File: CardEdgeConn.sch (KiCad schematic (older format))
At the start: 5 parts, among them J5 5-5530843-4, J6 Conn_01x03, J7 302-S101

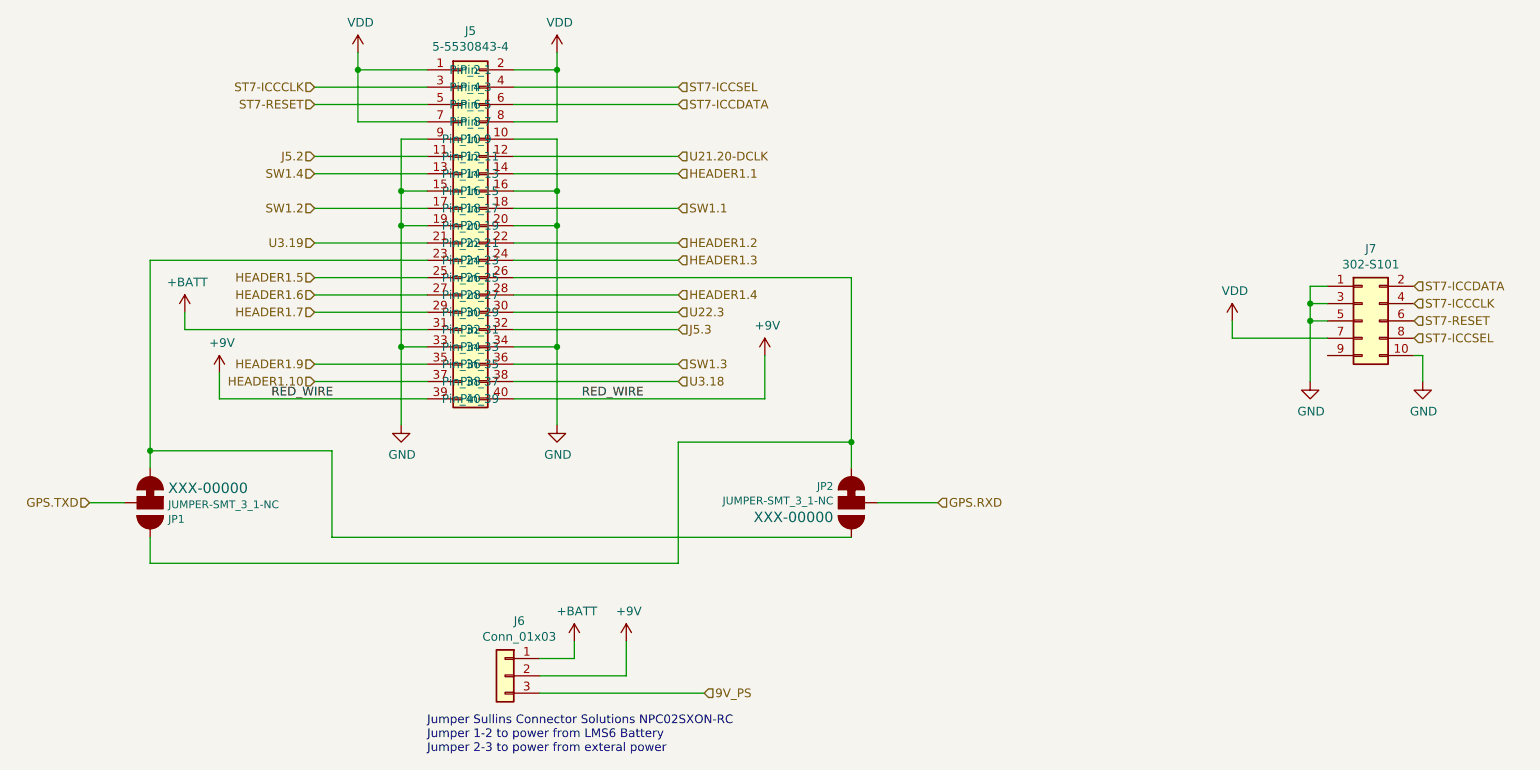
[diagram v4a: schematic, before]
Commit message: eFuse added
Added eFuse, LEDs, and addtional power configuration options.
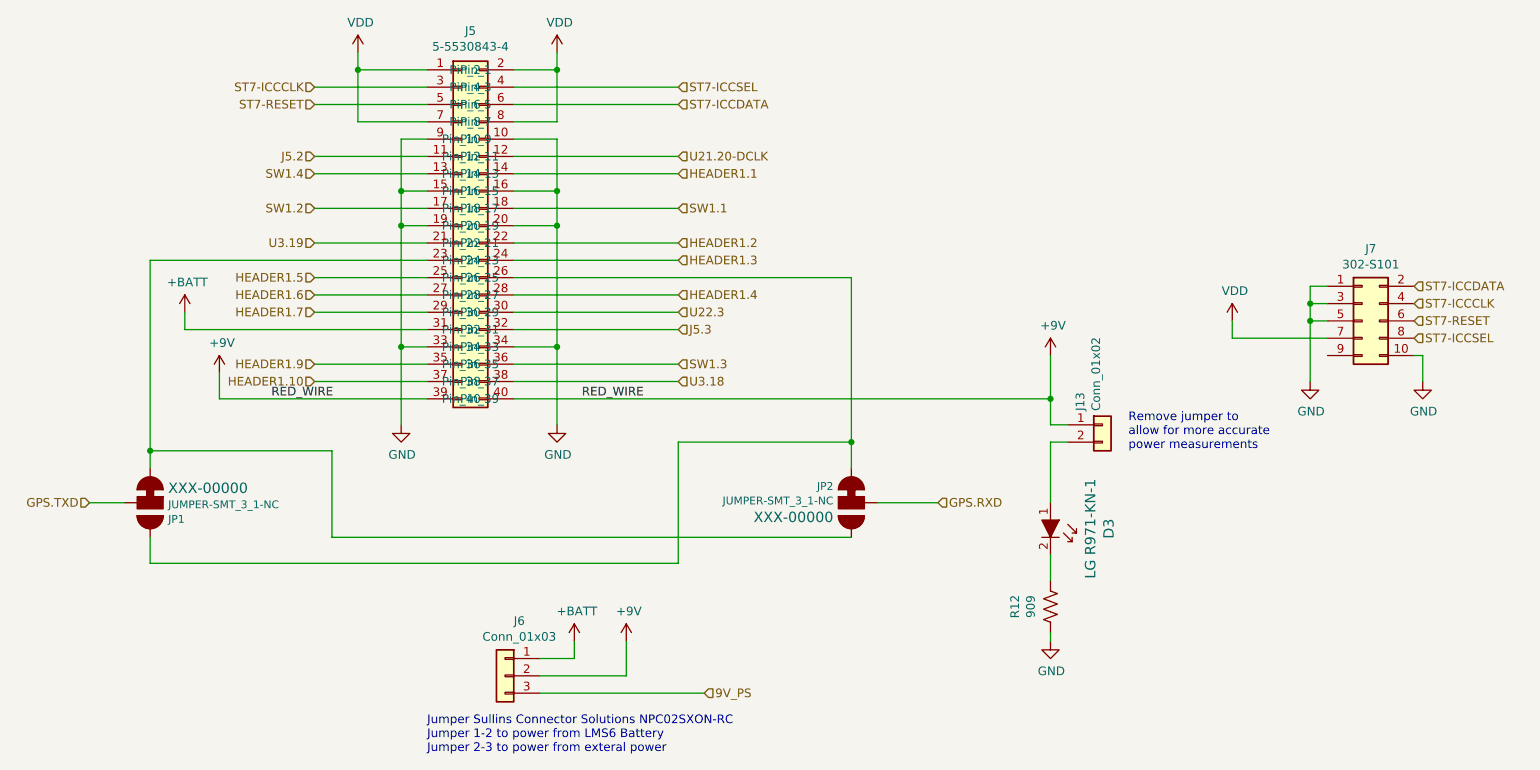
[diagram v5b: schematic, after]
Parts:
- added D3: LG R971-KN-1, digikey-footprints:0805, symbol dk_LED-Indication-Discrete:LH_R974-LP-1
- added J13: Conn_01x02, Connector_PinHeader_2.54mm:PinHeader_1x02_P2.54mm_Vertical, symbol Connector_Generic:Conn_01x02
- added R12: 909, Resistor_SMD:R_0805_2012Metric_Pad1.20x1.40mm_HandSolder, symbol Device:R_US
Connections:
- net +9V: now also J13.1 (Pin_1)
- net GND: now also R12.2
- new net: D3.1, J13.2 (Pin_2)
- new net: D3.2, R12.1
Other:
- note added: "Remove jumper to \nallow for more accurate\npower measurements"
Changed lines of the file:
@@
 $Descr A4 11693 8268
 encoding utf-8
-Sheet 4 4
-Title ""
-Date ""
-Rev ""
+Sheet 4 5
+Title "Card Connector"
+Date "2020-10-17"
+Rev "2"
 Comp ""
 Comment1 ""
@@
 L power:+9V #PWR?
 U 1 1 5F7D0952
-P 4850 2850
+P 6500 2850
 AR Path="/5F7D0952" Ref="#PWR?"  Part="1"
 AR Path="/5F7BE189/5F7D0952" Ref="#PWR?"  Part="1"
 AR Path="/5F7C6408/5F7D0952" Ref="#PWR0101"  Part="1"
-F 0 "#PWR0101" H 4850 2700 50  0001 C CNN
-F 1 "+9V" H 4865 3023 50  0000 C CNN
-F 2 "" H 4850 2850 50  0001 C CNN
-F 3 "" H 4850 2850 50  0001 C CNN
-	1    4850 2850
-	1    0    0    -1
-$EndComp
-Wire Wire Line
-	4850 3100 4850 2850
+F 0 "#PWR0101" H 6500 2700 50  0001 C CNN
+F 1 "+9V" H 6515 3023 50  0000 C CNN
+F 2 "" H 6500 2850 50  0001 C CNN
+F 3 "" H 6500 2850 50  0001 C CNN
+	1    6500 2850
+	1    0    0    -1
+$EndComp
+Wire Wire Line
+	6500 3100 6500 2850
 Wire Wire Line
 	4350 2600 3400 2600
@@
 Text Label 4150 3100 2    50   ~ 0
 RED_WIRE
-Wire Wire Line
-	3400 3100 4850 3100
 Wire Wire Line
 	4350 1300 3400 1300
@@
 Wire Wire Line
 	5350 3350 5350 2400
+Wire Wire Line
+	3400 3100 6500 3100
+$Comp
+L dk_LED-Indication-Discrete:LH_R974-LP-1 D?
+U 1 1 5F959F13
+P 6500 3900
+AR Path="/5F917C06/5F959F13" Ref="D?"  Part="1"
+AR Path="/5F8460BD/5F959F13" Ref="D?"  Part="1"
+AR Path="/5F7C6408/5F959F13" Ref="D3"  Part="1"
+F 0 "D3" H 6450 4237 60  0000 C CNN
+F 1 "LG R971-KN-1" H 6450 4131 60  0000 C CNN
+F 2 "digikey-footprints:0805" H 6700 4100 60  0001 L CNN
+F 3 "https://dammedia.osram.info/media/resource/hires/osram-dam-2493888/LH%20R974.pdf" H 6700 4200 60  0001 L CNN
+F 4 "475-1410-1-ND" H 6700 4300 60  0001 L CNN "Digi-Key_PN"
+F 5 "LG R971-KN-1" H 6700 4400 60  0001 L CNN "MPN"
+F 6 "Optoelectronics" H 6700 4500 60  0001 L CNN "Category"
+F 7 "LED Indication - Discrete" H 6700 4600 60  0001 L CNN "Family"
+F 8 "https://dammedia.osram.info/media/resource/hires/osram-dam-2493888/LH%20R974.pdf" H 6700 4700 60  0001 L CNN "DK_Datasheet_Link"
+F 9 "/product-detail/en/osram-opto-semiconductors-inc/LH-R974-LP-1/475-1415-1-ND/1802604" H 6700 4800 60  0001 L CNN "DK_Detail_Page"
+F 10 "LED GREEN DIFFUSED 0805 SMD" H 6700 4900 60  0001 L CNN "Description"
+F 11 "OSRAM Opto Semiconductors Inc." H 6700 5000 60  0001 L CNN "Manufacturer"
+F 12 "Active" H 6700 5100 60  0001 L CNN "Status"
+	1    6500 3900
+	0    1    1    0
+$EndComp
+$Comp
+L Device:R_US R?
+U 1 1 5F959F1B
+P 6500 4300
+AR Path="/5F8460BD/5F959F1B" Ref="R?"  Part="1"
+AR Path="/5F917C06/5F959F1B" Ref="R?"  Part="1"
+AR Path="/5F7C6408/5F959F1B" Ref="R12"  Part="1"
+F 0 "R12" V 6295 4300 50  0000 C CNN
+F 1 "909" V 6386 4300 50  0000 C CNN
+F 2 "Resistor_SMD:R_0805_2012Metric_Pad1.20x1.40mm_HandSolder" V 6540 4290 50  0001 C CNN
+F 3 "https://www.yageo.com/upload/media/product/productsearch/datasheet/rchip/PYu-RC_Group_51_RoHS_L_11.pdf" H 6500 4300 50  0001 C CNN
+F 4 "Yageo" V 6500 4300 50  0001 C CNN "Manufacturer"
+F 5 "RC0805FR-07909RL" V 6500 4300 50  0001 C CNN "MPN"
+	1    6500 4300
+	1    0    0    -1
+$EndComp
+Wire Wire Line
+	6500 4150 6500 4000
+$Comp
+L Connector_Generic:Conn_01x02 J?
+U 1 1 5F963A79
+P 6800 3250
+AR Path="/5F963A79" Ref="J?"  Part="1"
+AR Path="/5F7C6408/5F963A79" Ref="J13"  Part="1"
+F 0 "J13" V 6672 3330 50  0000 L CNN
+F 1 "Conn_01x02" V 6763 3330 50  0000 L CNN
+F 2 "Connector_PinHeader_2.54mm:PinHeader_1x02_P2.54mm_Vertical" H 6800 3250 50  0001 C CNN
+F 3 "~" H 6800 3250 50  0001 C CNN
+F 4 "Würth Elektronik" V 6800 3250 50  0001 C CNN "Manufacturer"
+F 5 "61300211121" V 6800 3250 50  0001 C CNN "MPN"
+	1    6800 3250
+	1    0    0    -1
+$EndComp
+Wire Wire Line
+	6500 3100 6500 3250
+Wire Wire Line
+	6500 3250 6600 3250
+Connection ~ 6500 3100
+Wire Wire Line
+	6600 3350 6500 3350
+Wire Wire Line
+	6500 3350 6500 3700
+Text Notes 6950 3400 0    50   ~ 0
+Remove jumper to \nallow for more accurate\npower measurements
+$Comp
+L power:GND #PWR023
+U 1 1 5F98BEEC
+P 6500 4500
+F 0 "#PWR023" H 6500 4250 50  0001 C CNN
+F 1 "GND" H 6505 4327 50  0000 C CNN
+F 2 "" H 6500 4500 50  0001 C CNN
+F 3 "" H 6500 4500 50  0001 C CNN
+	1    6500 4500
+	1    0    0    -1
+$EndComp
+Wire Wire Line
+	6500 4450 6500 4500
 $EndSCHEMATC

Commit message: Fixed J6 footprint and MPN info
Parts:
- J6: footprint (none) -> Connector_PinHeader_2.54mm:PinHeader_1x03_P2.54mm_Vertical; MPN (none) -> 61300311121; Manufacturer (none) -> Würth Elektronik
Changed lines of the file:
@@
 Wire Wire Line
 	3750 4600 3550 4600
-$Comp
-L Connector_Generic:Conn_01x03 J6
-U 1 1 5F8CD356
-P 3350 4700
-F 0 "J6" H 3268 5017 50  0000 C CNN
-F 1 "Conn_01x03" H 3268 4926 50  0000 C CNN
-F 2 "" H 3350 4700 50  0001 C CNN
-F 3 "~" H 3350 4700 50  0001 C CNN
-	1    3350 4700
-	-1   0    0    -1
-$EndComp
 Text HLabel 4500 4800 2    50   Input ~ 0
 9V_PS
@@
 Wire Wire Line
 	6500 4450 6500 4500
+$Comp
+L Connector_Generic:Conn_01x03 J6
+U 1 1 5F9ABDCE
+P 3350 4700
+AR Path="/5F7C6408/5F9ABDCE" Ref="J6"  Part="1"
+AR Path="/5F9ABDCE" Ref="J?"  Part="1"
+F 0 "J6" H 3268 5017 50  0000 C CNN
+F 1 "Conn_01x03" H 3268 4926 50  0000 C CNN
+F 2 "Connector_PinHeader_2.54mm:PinHeader_1x03_P2.54mm_Vertical" H 3350 4700 50  0001 C CNN
+F 3 "https://katalog.we-online.de/em/datasheet/6130xx11121.pdf" H 3350 4700 50  0001 C CNN
+F 4 "Würth Elektronik" H 3350 4700 50  0001 C CNN "Manufacturer"
+F 5 "61300311121" H 3350 4700 50  0001 C CNN "MPN"
+	1    3350 4700
+	-1   0    0    -1
+$EndComp
 $EndSCHEMATC
